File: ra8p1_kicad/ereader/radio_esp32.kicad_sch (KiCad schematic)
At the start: 3 parts, among them U3 ESP32-C6-WROOM-1-N8

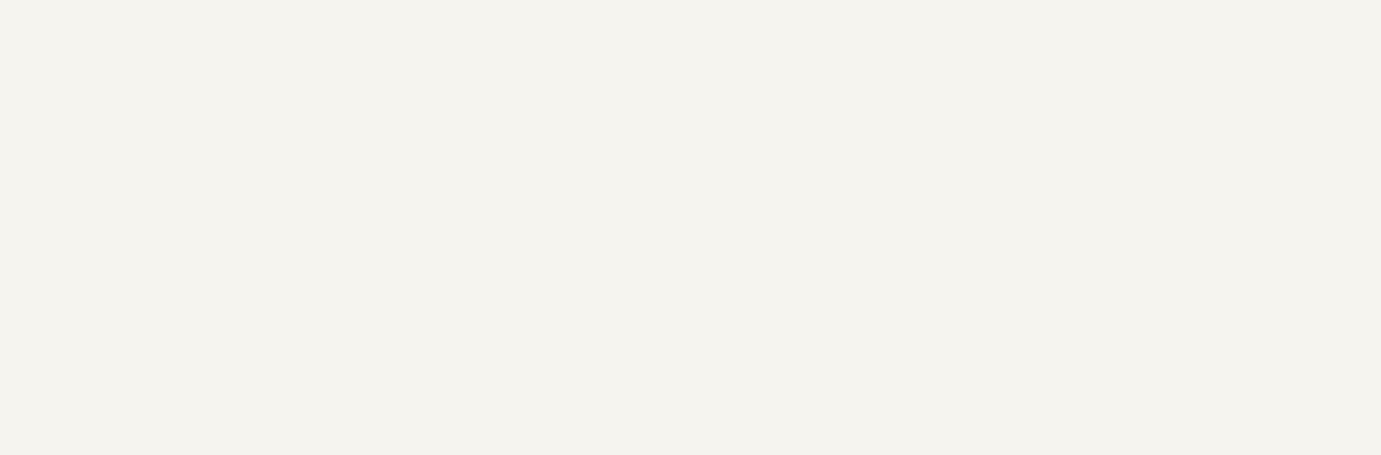
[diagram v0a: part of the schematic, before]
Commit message: Add sourced radio load switch and linked electrical screening
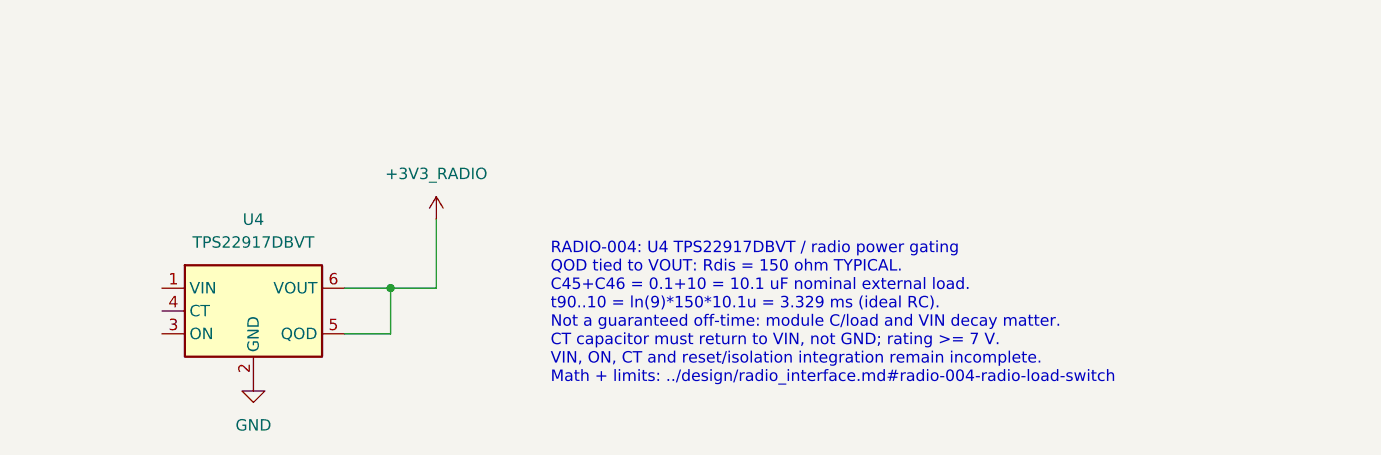
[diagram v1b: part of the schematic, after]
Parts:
- added U4: TPS22917DBVT, Package_TO_SOT_SMD:SOT-23-6, symbol Power_Devices:TPS22917DBVT
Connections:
- net +3V3_RADIO: now also U4.5 (QOD), U4.6 (VOUT)
- net GND: now also U4.2 (GND)
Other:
- note added: "RADIO-004: U4 TPS22917DBVT / radio power gating QOD tied to VOUT: Rdis = 150 ohm TYPICAL. C45+C46 = 0.1+10 = 10.1 uF nominal external load. t90..10 = ln(9)*150*10.1u = 3.329 ms (ideal RC). Not a guaranteed off-time: module C/load and VIN decay matter. CT capacitor must return to VIN, not GND; rating >= 7 V. VIN, ON, CT and reset/isolation integration remain incomplete. Math + limits: ../design/ra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"

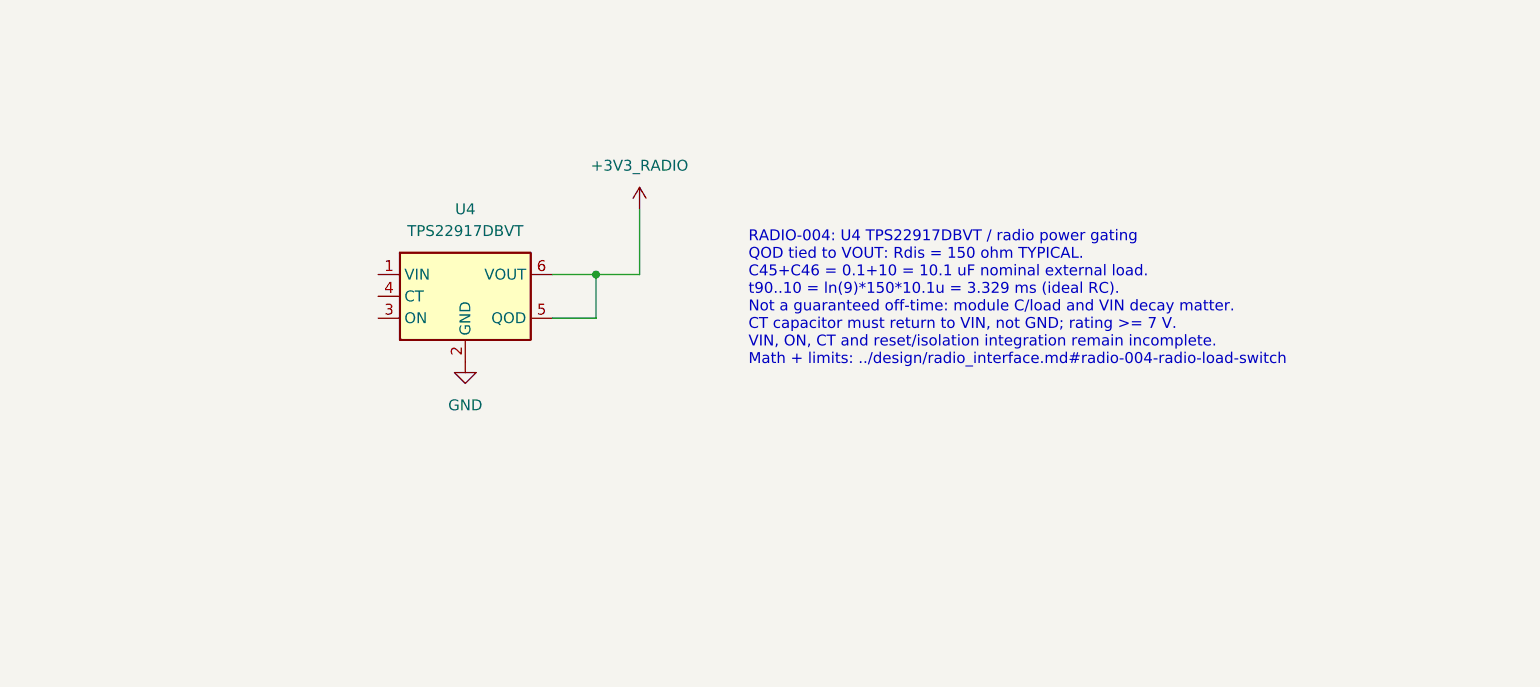
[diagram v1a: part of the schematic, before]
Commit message: Connect radio switch input bypass and document capacitance scope
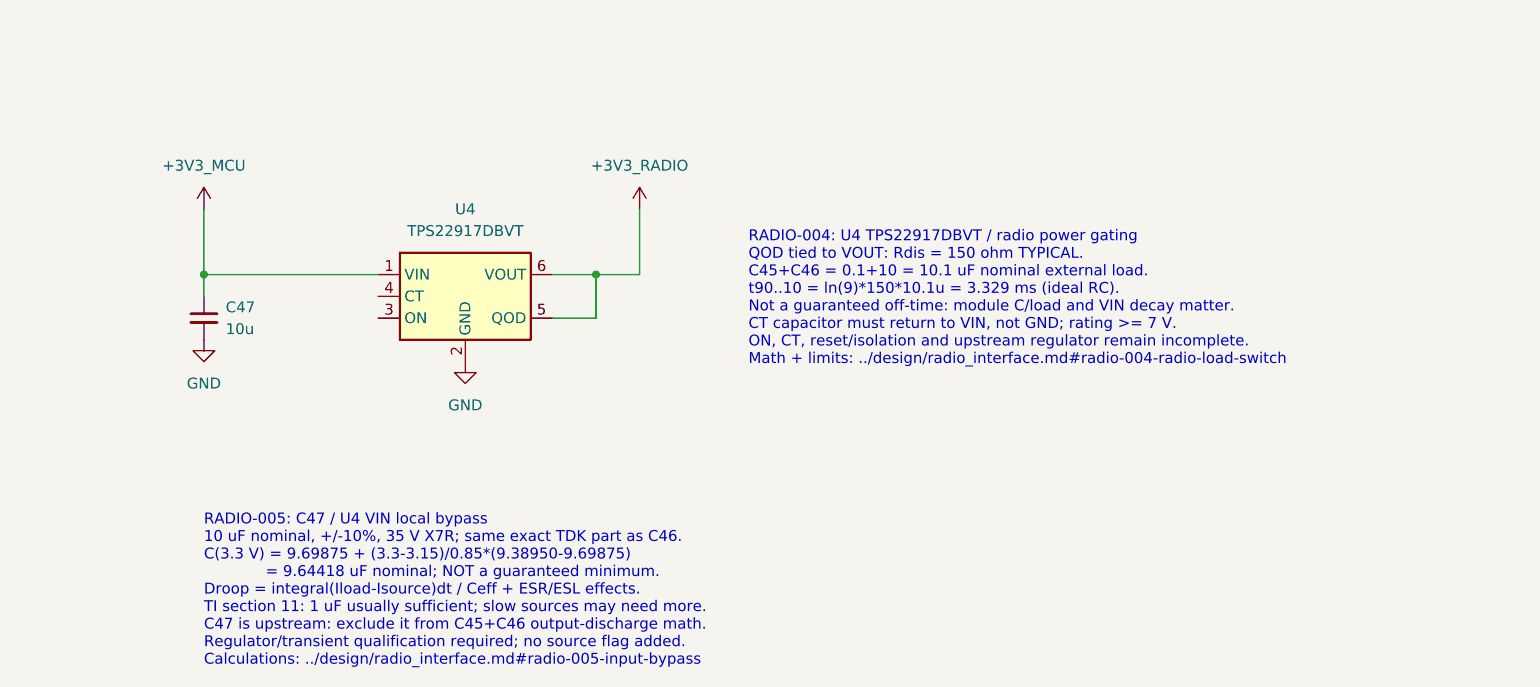
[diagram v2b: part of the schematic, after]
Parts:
- added C47: 10u, symbol Device:C_Small
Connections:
- net GND: now also C47.2
- net +3V3_MCU: now reaches U4.1 (VIN)
- net +3V3_MCU: now also C47.1
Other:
- note added: "RADIO-004: U4 TPS22917DBVT / radio power gating QOD tied to VOUT: Rdis = 150 ohm TYPICAL. C45+C46 = 0.1+10 = 10.1 uF nominal external load. t90..10 = ln(9)*150*10.1u = 3.329 ms (ideal RC). Not a guaranteed off-time: module C/load and VIN decay matter. CT capacitor must return to VIN, not GND; rating >= 7 V. ON, CT, reset/isolation and upstream regulator remain incomplete. Math + limits: ../design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"
- note added: "RADIO-005: C47 / U4 VIN local bypass 10 uF nominal, +/-10%, 35 V X7R; same exact TDK part as C46. C(3.3 V) = 9.69875 + (3.3-3.15)/0.85*(9.38950-9.69875) = 9.64418 uF nominal; NOT a guaranteed minimum. Droop = integral(Iload-Isource)dt / Ceff + ESR/ESL effects. TI section 11: 1 uF usually sufficient; slow sources may need more. C47 is upstream: exclude it from C45+C46 output-discharge math. Regula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"
- note removed: "RADIO-004: U4 TPS22917DBVT / radio power gating QOD tied to VOUT: Rdis = 150 ohm TYPICAL. C45+C46 = 0.1+10 = 10.1 uF nominal external load. t90..10 = ln(9)*150*10.1u = 3.329 ms (ideal RC). Not a guaranteed off-time: module C/load and VIN decay matter. CT capacitor must return to VIN, not GND; rating >= 7 V. VIN, ON, CT and reset/isolation integration remain incomplete. Math + limits: ../design/ra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"

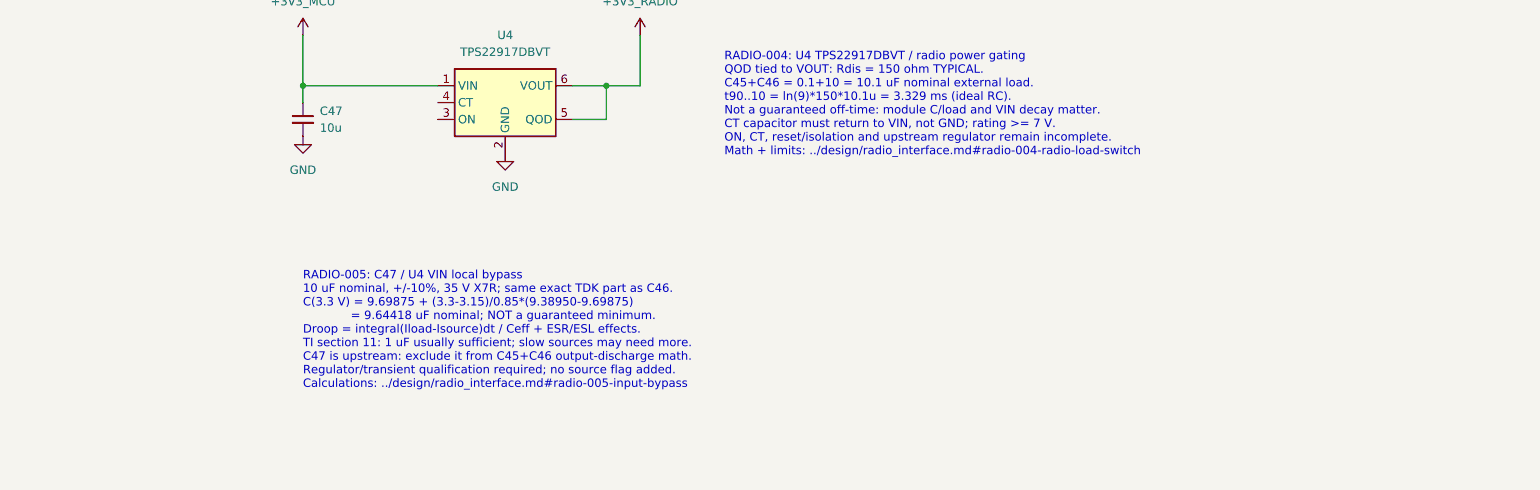
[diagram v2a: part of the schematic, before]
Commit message: Add radio enable divider with verified logic-level screening
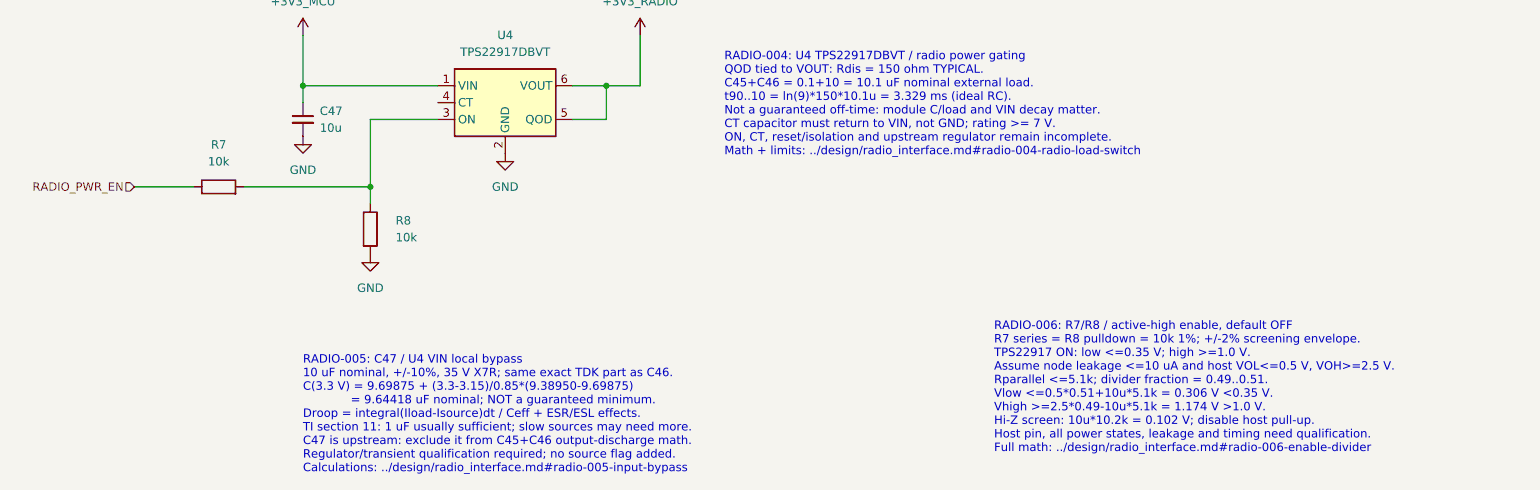
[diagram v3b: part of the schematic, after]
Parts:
- added R7, R8: 10k, symbol Device:R
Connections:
- net GND: now also R8.2
- net at U4.3 (ON): now also R7.2, R8.1
- new net RADIO_PWR_EN: R7.1
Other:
- note added: "RADIO-006: R7/R8 / active-high enable, default OFF R7 series = R8 pulldown = 10k 1%; +/-2% screening envelope. TPS22917 ON: low <=0.35 V; high >=1.0 V. Assume node leakage <=10 uA and host VOL<=0.5 V, VOH>=2.5 V. Rparallel <=5.1k; divider fraction = 0.49..0.51. Vlow <=0.5*0.51+10u*5.1k = 0.306 V <0.35 V. Vhigh >=2.5*0.49-10u*5.1k = 1.174 V >1.0 V. Hi-Z screen: 10u*10.2k = 0.102 V; disable host pu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"

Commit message: Add radio slew-rate capacitor and linked timing calculations
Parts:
- added C48: 1n, symbol Device:C_Small
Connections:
- net +3V3_MCU: now also C48.1
- net at U4.4 (CT): now also C48.2
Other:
- note added: "RADIO-004: U4 TPS22917DBVT / radio power gating QOD tied to VOUT: Rdis = 150 ohm TYPICAL. C45+C46 = 0.1+10 = 10.1 uF nominal external load. t90..10 = ln(9)*150*10.1u = 3.329 ms (ideal RC). Not a guaranteed off-time: module C/load and VIN decay matter. C48 connects CT to VIN, not GND; 50 V rating >=7 V required. Host control, reset/isolation and upstream regulator remain incomplete. Math + limits: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"
- note added: "RADIO-007: C48 / CT slew-rate control, TDK C1608NP01H102J080AA 1nF +/-5%, 50 V NP0; CT-to-VIN, NOT CT-to-GND. TI 3.6 V / 25 C TYPICAL table point, not guaranteed at 3.3 V: Slew = 1900/1000 = 1.9 mV/us; tON = 3.8*1000 = 3.8 ms. tR(10..90%) = 1.6*1000 = 1.6 ms (TI test load). C45+C46 = 10.1 uF nominal: Icap = C*dV/dt = 19.19 mA. Open-CT comparison: 10.1u*44mV/us = 444.4 mA (typical). Total inrush a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"
- note removed: "RADIO-004: U4 TPS22917DBVT / radio power gating QOD tied to VOUT: Rdis = 150 ohm TYPICAL. C45+C46 = 0.1+10 = 10.1 uF nominal external load. t90..10 = ln(9)*150*10.1u = 3.329 ms (ideal RC). Not a guaranteed off-time: module C/load and VIN decay matter. CT capacitor must return to VIN, not GND; rating >= 7 V. ON, CT, reset/isolation and upstream regulator remain incomplete. Math + limits: ../design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"
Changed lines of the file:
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@@
 		(comment 1 "Incomplete electrical design - not for manufacture")
 	)
-	(text "RADIO-004: U4 TPS22917DBVT / radio power gating\nQOD tied to VOUT: Rdis = 150 ohm TYPICAL.\nC45+C46 = 0.1+10 = 10.1 uF nominal external load.\nt90..10 = ln(9)*150*10.1u = 3.329 ms (ideal RC).\nNot a guaranteed off-time: module C/load and VIN decay matter.\nCT capacitor must return to VIN, not GND; rating >= 7 V.\nON, CT, reset/isolation and upstream regulator remain incomplete.\nMath + limits: ../design/radio_interface.md#radio-004-radio-load-switch"
+	(text "RADIO-004: U4 TPS22917DBVT / radio power gating\nQOD tied to VOUT: Rdis = 150 ohm TYPICAL.\nC45+C46 = 0.1+10 = 10.1 uF nominal external load.\nt90..10 = ln(9)*150*10.1u = 3.329 ms (ideal RC).\nNot a guaranteed off-time: module C/load and VIN decay matter.\nC48 connects CT to VIN, not GND; 50 V rating >=7 V required.\nHost control, reset/isolation and upstream regulator remain incomplete.\nMath + limits: ../design/radio_interface.md#radio-004-radio-load-switch"
 		(exclude_from_sim no)
 		(at 187.96 144.78 0)
@@
 		)
 	)
+	(text "RADIO-007: C48 / CT slew-rate control, TDK C1608NP01H102J080AA\n1nF +/-5%, 50 V NP0; CT-to-VIN, NOT CT-to-GND.\nTI 3.6 V / 25 C TYPICAL table point, not guaranteed at 3.3 V:\nSlew = 1900/1000 = 1.9 mV/us; tON = 3.8*1000 = 3.8 ms.\ntR(10..90%) = 1.6*1000 = 1.6 ms (TI test load).\nC45+C46 = 10.1 uF nominal: Icap = C*dV/dt = 19.19 mA.\nOpen-CT comparison: 10.1u*44mV/us = 444.4 mA (typical).\nTotal inrush also includes module C/load and future rail parts.\nNot a current limiter or reset delay; startup qualification required.\nFull math: ../design/radio_interface.md#radio-007-slew-rate-capacitor"
+		(exclude_from_sim no)
+		(at 228.6 228.6 0)
+		(effects
+			(font
+				(size 1.27 1.27)
+			)
+			(justify left top)
+			(href "https://github.com/bsikar/ra8-firmware/blob/design/ereader-circuit/ra8p1_kicad/design/radio_interface.md#radio-007-slew-rate-capacitor")
+		)
+	)
 	(text "RADIO-006: R7/R8 / active-high enable, default OFF\nR7 series = R8 pulldown = 10k 1%; +/-2% screening envelope.\nTPS22917 ON: low <=0.35 V; high >=1.0 V.\nAssume node leakage <=10 uA and host VOL<=0.5 V, VOH>=2.5 V.\nRparallel <=5.1k; divider fraction = 0.49..0.51.\nVlow <=0.5*0.51+10u*5.1k = 0.306 V <0.35 V.\nVhigh >=2.5*0.49-10u*5.1k = 1.174 V >1.0 V.\nHi-Z screen: 10u*10.2k = 0.102 V; disable host pull-up.\nHost pin, all power states, leakage and timing need qualification.\nFull math: ../design/radio_interface.md#radio-006-enable-divider"
 		(exclude_from_sim no)
@@
 	)
 	(junction
+		(at 124.46 152.4)
+		(diameter 0)
+		(color 0 0 0 0)
+	)
+	(junction
 		(at 134.62 165.1)
 		(diameter 0)
@@
 	(wire
 		(pts
+			(xy 137.16 152.4) (xy 144.78 152.4)
+		)
+		(stroke
+			(width 0)
+			(type default)
+		)
+	)
+	(wire
+		(pts
 			(xy 139.7 78.74) (xy 154.94 78.74)
 		)
@@
 		(pts
 			(xy 99.06 165.1) (xy 107.95 165.1)
+		)
+		(stroke
+			(width 0)
+			(type default)
+		)
+	)
+	(wire
+		(pts
+			(xy 124.46 152.4) (xy 132.08 152.4)
 		)
 		(stroke
@@
 	)
 	(symbol
-		(lib_name "+3V3_1")
 		(lib_id "power:+3V3")
 		(at 124.46 142.24 0)
@@
 					(unit 1)
 				)
+			)
+		)
+	)
+	(symbol
+		(lib_id "Device:C_Small")
+		(at 134.62 152.4 90)
+		(unit 1)
+		(body_style 1)
+		(exclude_from_sim no)
+		(in_bom yes)
+		(on_board yes)
+		(in_pos_files yes)
+		(dnp no)
+		(fields_autoplaced yes)
+		(property "Reference" "C48"
+			(at 134.6263 146.05 90)
+			(show_name no)
+			(do_not_autoplace no)
+			(effects
+				(font
+					(size 1.27 1.27)
+				)
+			)
+		)
+		(property "Value" "1n"
+			(at 134.6263 148.59 90)
+			(show_name no)
+			(do_not_autoplace no)
+			(effects
+				(font
+					(size 1.27 1.27)
+				)
+			)
+		)
+		(property "Footprint" ""
+			(at 134.62 152.4 0)
+			(hide yes)
+			(show_name no)
+			(do_not_autoplace no)
+			(effects
+				(font
+					(size 1.27 1.27)
+				)
+			)
+		)
+		(property "Datasheet" "https://product.tdk.com/en/search/capacitor/ceramic/mlcc/info?part_no=C1608NP01H102J080AA"
+			(at 134.62 152.4 0)
+			(hide yes)
+			(show_name no)
+			(do_not_autoplace no)
+			(effects
+				(font
+					(size 1.27 1.27)
+				)
+			)
+		)
+		(property "Description" "TDK C1608NP01H102J080AA; 1nF +/-5%, 50V NP0; U4 CT-to-VIN timing capacitor. RADIO-007 typical timing screen, not a guaranteed reset delay."
+			(at 134.62 152.4 0)
+			(hide yes)
+			(show_name no)
+			(do_not_autoplace no)
+			(effects
+				(font
+					(size 1.27 1.27)
+				)
+			)
+		)
+		(property "DigiKey_Part_Number" "445-14055-1-ND"
+			(at 134.62 152.4 0)
+			(hide yes)
+			(show_name no)
+			(do_not_autoplace no)
+			(effects
+				(font
+					(size 1.27 1.27)
+				)
+			)
+		)
+		(property "DigiKey_URL" "https://www.digikey.com/en/products/detail/tdk/C1608NP01H102J080AA/3955721"
+			(at 134.62 152.4 0)
+			(hide yes)
+			(show_name no)
+			(do_not_autoplace no)
+			(effects
+				(font
+					(size 1.27 1.27)
+				)
+			)
+		)
+		(property "Manufacturer_Name" "TDK"
+			(at 134.62 152.4 0)
+			(hide yes)
+			(show_name no)
+			(do_not_autoplace no)
+			(effects
+				(font
+					(size 1.27 1.27)
+				)
+			)
+		)
+		(property "Manufacturer_Part_Number" "C1608NP01H102J080AA"
+			(at 134.62 152.4 0)
+			(hide yes)
+			(show_name no)
+			(do_not_autoplace no)
+			(effects
+				(font
+					(size 1.27 1.27)
+				)
+			)
+		)
+		(property "Procurement_Status" "Selected - initial slew-rate screen; full startup and transient qualification open; footprint deferred."
+			(at 134.62 152.4 0)
+			(hide yes)
+			(show_name no)
+			(do_not_autoplace no)
+			(effects
+				(font
+					(size 1.27 1.27)
+				)
+			)
+		)
+		(property "Selection_Basis" "RADIO-007: 1nF NP0 50V from CT to VIN; TI >=7V rating met. Typical 3.6V table: slew 1900/1000=1.9mV/us, tON=3.8ms. Complete output C and upstream transient budget remain open."
+			(at 134.62 152.4 0)
+			(hide yes)
+			(show_name no)
+			(do_not_autoplace no)
+			(effects
+				(font
+					(size 1.27 1.27)
+				)
+			)
+		)
+		(property "Sourcing_Snapshot" "2026-09-05: TDK Production; DigiKey Active, 27277 stock, 24 weeks; USD 0.22/0.125/0.078 at 1/10/100. Recheck before ordering."
+			(at 134.62 152.4 0)
+			(hide yes)
+			(show_name no)
+			(do_not_autoplace no)
+			(effects
+				(font
+					(size 1.27 1.27)
+				)
+			)
+		)
+		(pin "2"
+		)
+		(pin "1"
+		)
+		(instances
+			(project "ereader_rev1"
+				(path "/0586cc51-9c57-495b-a0c9-c29ba0d48166/9b84c337-6879-4714-899e-3993bcc30b88"
+					(reference "C48")
+					(unit 1)
+				)

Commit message: Place sourced SPI translator and connect its supply domains
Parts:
- added U5: TXU0304PWR, symbol Power_Devices:TXU0304PWR
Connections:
- net +3V3_MCU: now also U5.1 (VCCA)
- net +3V3_RADIO: now also U5.14 (VCCB)
- net GND: now also U5.7 (GND)
